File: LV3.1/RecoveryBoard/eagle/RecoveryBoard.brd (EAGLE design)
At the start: 120.9 x 54.6 mm, 88 parts, among them IC1 BD62120AEFJ-E2, Q6 MOSFET-PCH-SOT23-6, U1 STM32F042K6, U10 TPS63070, Y1 ECS-160-10-36Q-ES-TR

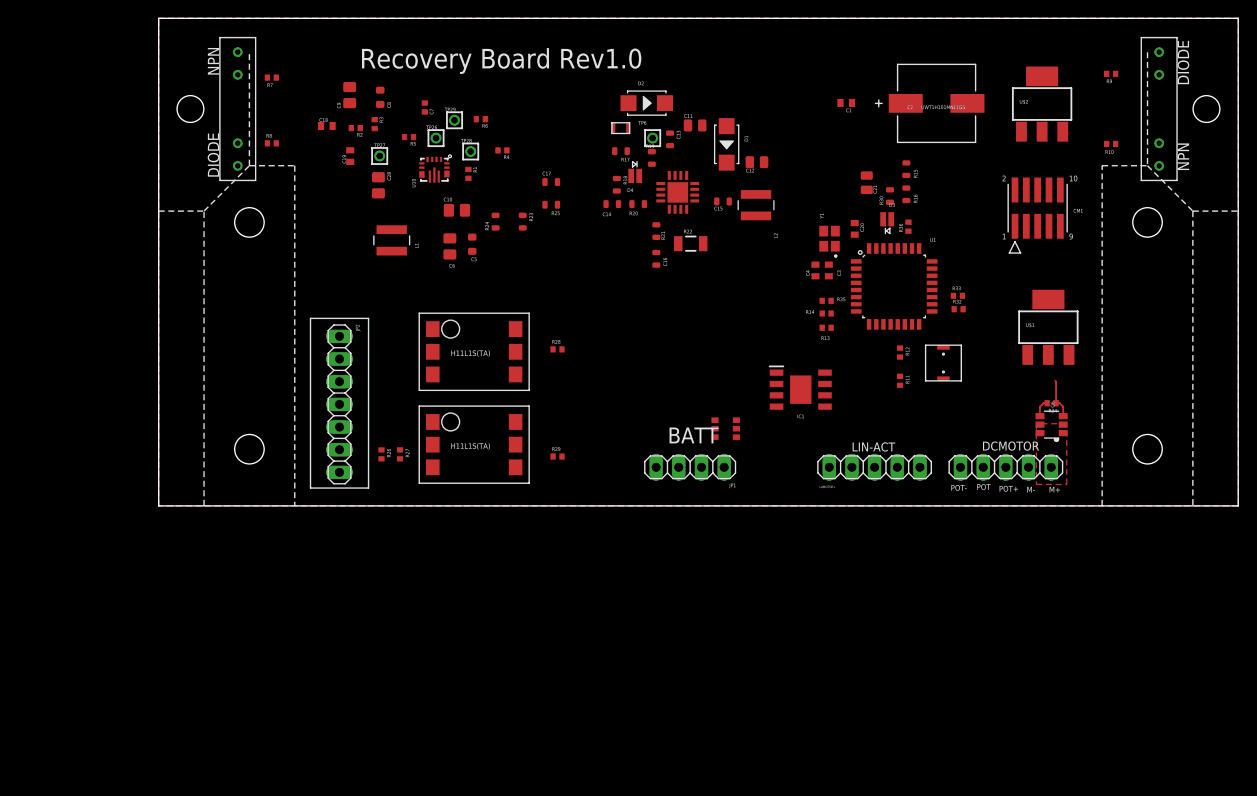
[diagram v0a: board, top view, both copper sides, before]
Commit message: OCD on package sizes 0603 for normal caps and resistors; 0805 for large caps, and larger yet for larger caps.
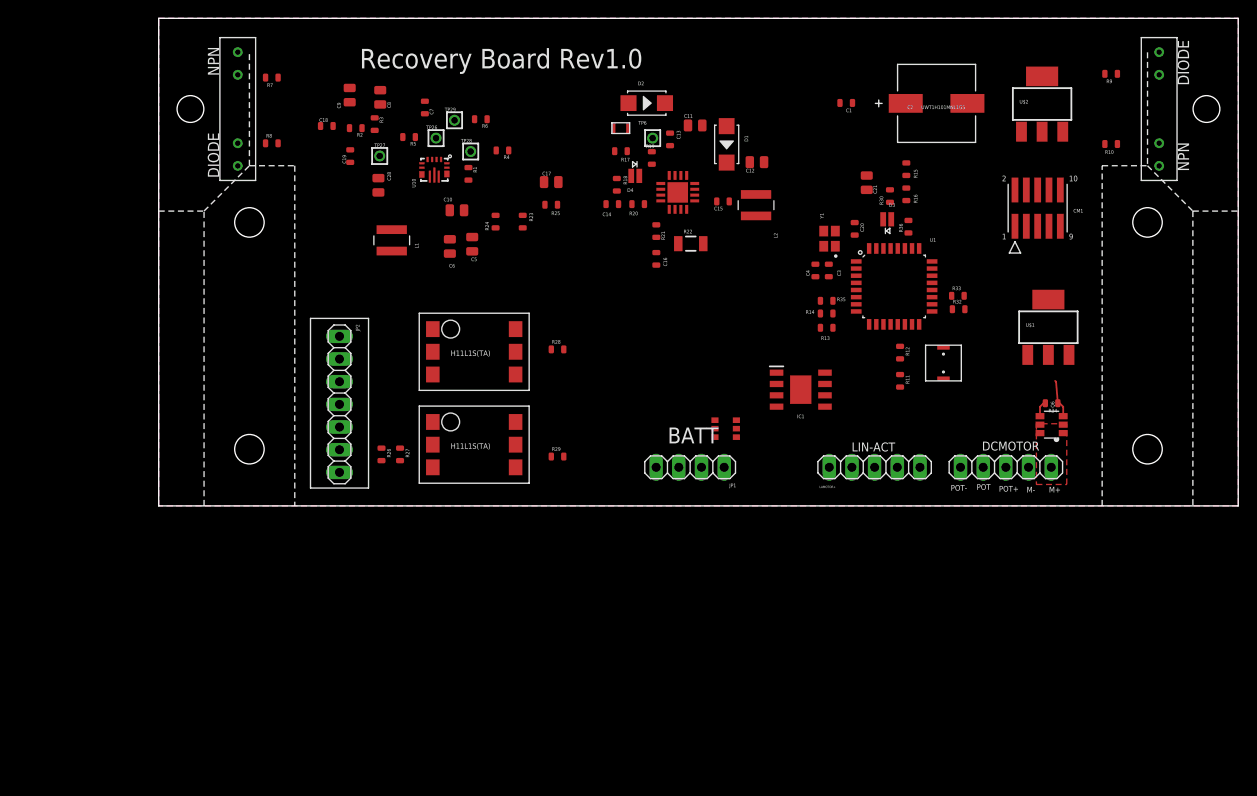
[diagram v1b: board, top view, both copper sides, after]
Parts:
- C1, C18, C19, C20, C3, C4: device rcl:C0402 -> oresat-rcl:.0603-C-NOSILK
- C10, C28, C6, C9: device oresat-rcl:.0805-B-NOSILK -> oresat-rcl:.0805-C-NOSILK
- C17: device oresat-rcl:.0603-C-NOSILK -> oresat-rcl:.0805-C-NOSILK
- C5, C8: device oresat-rcl:.0603-B-NOSILK -> oresat-rcl:.0805-C-NOSILK
- C7, R1, R2, R3, R4, R5, R6: device rcl_custom:.0402-B-NOSILK -> oresat-rcl:.0603-C-NOSILK
- R10, R11, R12, R13, R14, R26, R27, R28, R29, R32, R33, R34, R35, R36, R7, R8, R9: device rcl:R0402 -> oresat-rcl:.0603-C-NOSILK

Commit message: beginning routing and placement
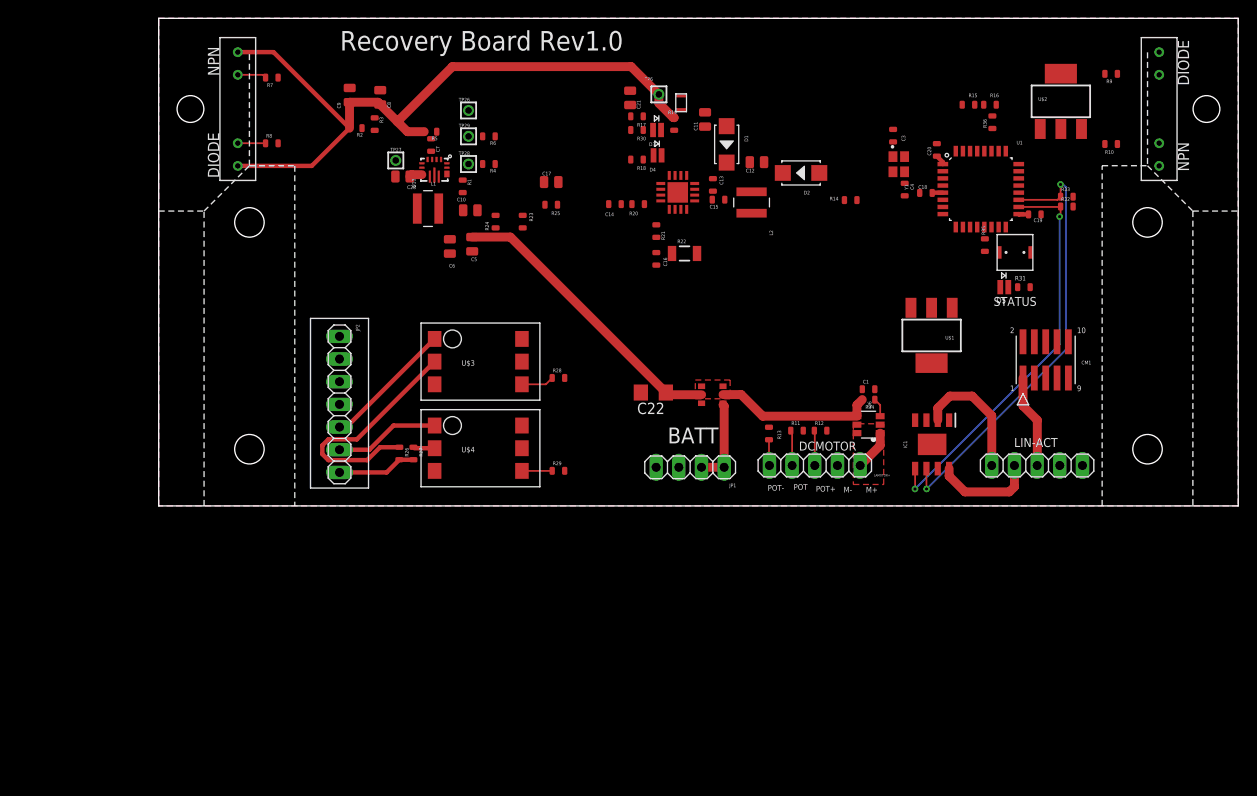
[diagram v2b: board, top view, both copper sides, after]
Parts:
- removed C2: UWT1H101MNL1GS, UWT1H101MNL1GS:PCAP_8X10-ELECT
- added C22: 100uF, oresat-rcl:C1206
- added D5: X-QE, D-Cree-XQE-LED:X-QE
- added R31: 220, oresat-rcl:.0603-C-NOSILK
- U$3, U$4: value H11L1S(TA) -> H11F1SR2M; device Q--H11L1S(TA)--OptoIsolator:H11L1S(TA) -> Q--H11F1SR2M--OptoIsolator:H11F1SR2M
- moved C19 76.9 mm to (98.1, 32.6), turned to 0 degrees
- moved C18 67.5 mm to (85.9, 35.0)
- moved C1 32.2 mm to (79.5, 13.1), turned to 0 degrees
- moved R30 29.3 mm to (53.6, 42.1), turned to 180 degrees
- moved C21 28.2 mm to (52.8, 45.7)
- moved D3 27.6 mm to (55.8, 42.1), turned to 0 degrees
- moved J1 21.4 mm to (73.5, 4.53)
- moved R34 20.5 mm to (79.5, 11.9)
- moved Q6 20.5 mm to (79.5, 9.10)
- moved D2 19.0 mm to (71.9, 37.3), turned to 180 degrees
- moved R35 18.8 mm to (92.5, 29.2), turned to 270 degrees
- moved J2 18.2 mm to (98.4, 4.53)
- moved CM1 17.0 mm to (99.3, 16.4)
- moved C3 16.7 mm to (82.2, 41.5)
- moved R32 16.7 mm to (101.7, 33.5)
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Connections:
- removed net LED: U1.26
- removed net N$25: R28.1, U$3.GND
- removed net N$29: R29.1, U$4.GND
- new net N$15: D5.ANODE, U1.14
- new net N$4: D5.CATHODE, R31.1
- net +12V: now also C22.1; no longer C2.1
- net 3.3V: now also U$3.IN, U$4.IN; no longer U$3.VCC, U$4.VCC
- net ARM-IN: now also JP2.2; no longer JP2.6
- net ARM-OUT: now also JP2.1; no longer JP2.7
- net CHUTE: now also JP2.5; no longer JP2.3
- net DCMDIR: no longer U1.13
- net DCM_ON: now also U1.13; no longer U1.6
- net DCM_PWM: no longer U1.14
- net DCM_SPEED: now also U1.6; no longer U1.7
- net DROGUE: now also JP2.6; no longer JP2.4
- net GND: now also C22.2, JP2.4, R31.2; no longer C2.2, JP2.2
- net ISO-CHUTE: now also R28.1, U$3.OUT, U1.9; no longer U$3.VO, U1.11
- net ISO-DROGUE: now also R29.1, U$4.OUT, U1.10; no longer U$4.VO, U1.12
- net SENSOR1: no longer U1.9
- net SENSOR2: no longer U1.10
- net T_GND: now also JP2.7; no longer JP2.5
- net VUMB: now also JP2.3; no longer JP2.1
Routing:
- net 3.3V: track 0.00 -> 94.8 mm
- net IN2: track 0.00 -> 49.5 mm, vias 0 -> 2
- net +12V: track 1.82 -> 51.1 mm
- net IN1: track 0.00 -> 45.4 mm, vias 0 -> 2
- net N$7: track 0.00 -> 26.9 mm
- net CHUTE: track 0.00 -> 14.7 mm
- net LAMOTOR+: track 0.00 -> 14.4 mm
- net DROGUE: track 0.00 -> 11.8 mm
- net LAMOTOR-: track 0.00 -> 11.5 mm
- net VBAT: track 0.00 -> 9.58 mm
- net T_GND: track 0.00 -> 8.87 mm
- net DCM+: track 0.00 -> 4.55 mm
- net DCM_PWM: track 0.00 -> 3.97 mm
- net DCMDIR: track 0.00 -> 3.93 mm
- net ISO-CHUTE: track 0.00 -> 3.68 mm
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- added copper zone on layer 1, net +12V
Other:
- board text added: "STATUS"
- board text removed: "SPS"
- board text removed: "this cap is too big"

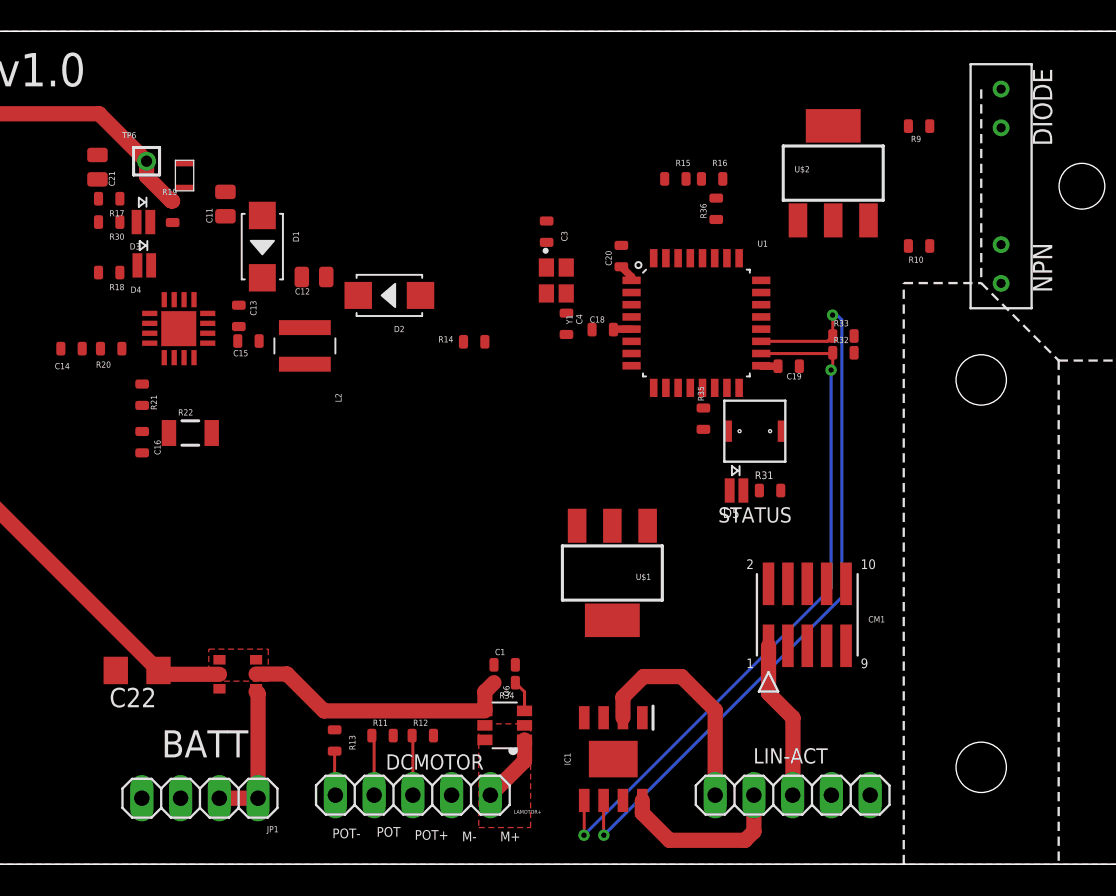
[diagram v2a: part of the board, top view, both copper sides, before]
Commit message: beginning routing and placement
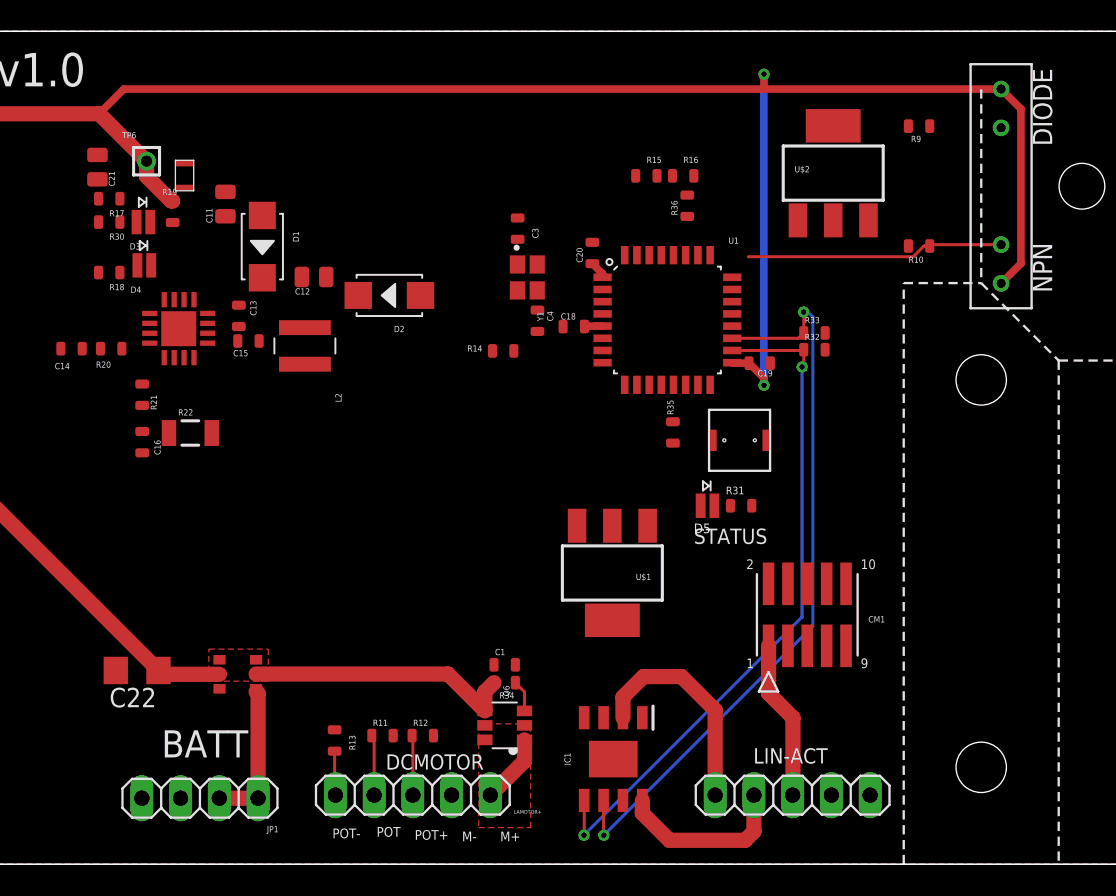
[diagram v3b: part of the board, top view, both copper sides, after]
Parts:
- moved R35 2.19 mm to (90.5, 28.3)
- moved D5 2.15 mm to (92.8, 23.5)
- moved R31 2.15 mm to (95.0, 23.5)
- moved R14 1.99 mm to (79.4, 33.6)
- moved C18 1.91 mm to (84.0, 35.2)
- moved C19 1.91 mm to (96.2, 32.9)
- moved C20 1.91 mm to (85.2, 40.1)
- moved C3 1.91 mm to (80.3, 41.7)
- moved R36 1.91 mm to (91.5, 43.2)
- moved Y1 1.91 mm to (81.0, 38.5)
- moved C4 1.91 mm to (81.7, 35.6)
- moved R15 1.91 mm to (88.8, 45.1)
- moved R16 1.91 mm to (91.2, 45.1)
- moved U1 1.91 mm to (90.2, 35.7)
- moved R32 1.91 mm to (99.8, 33.7)
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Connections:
- net BATT_READ: now also U1.29; no longer U1.28
- net DCMDIR: now also U1.12
- net DCM_PWM: now also U1.11
- net SENSOR1: now also U1.28
- net SENSOR2: now also U1.27
- net SENSOR_ON: now also U1.26; no longer U1.27
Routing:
- net 3.3V: track 94.8 -> 191.7 mm, vias 0 -> 2
- net SENSOR2: track 0.00 -> 16.9 mm
- net IN1: track 45.4 -> 44.8 mm
- net IN2: track 49.5 -> 48.9 mm

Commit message: finished routing
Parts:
- moved C20 0.53 mm to (85.8, 40.0), turned to 0 degrees
- moved C5 0.36 mm to (35.3, 29.0)
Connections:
- net N$3 renamed OSC_IN
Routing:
- net N$27: track 0.00 -> 131.4 mm, vias 0 -> 2
- net 3.3V: track 191.7 -> 313.9 mm, vias 2 -> 3
- net VBAT: track 9.58 -> 109.3 mm, vias 0 -> 4
- net SENSOR1: track 3.24 -> 89.3 mm, vias 0 -> 2
- net VUMB: track 0.00 -> 73.1 mm, vias 0 -> 1
- net ISO-DROGUE: track 3.39 -> 62.4 mm, vias 0 -> 2
- net POT_OUT_AN: track 0.00 -> 57.9 mm
- net ISO-CHUTE: track 3.68 -> 54.9 mm, vias 0 -> 2
- net ACOK: track 0.00 -> 45.2 mm, vias 0 -> 2
- net DCM_SPEED: track 0.00 -> 36.8 mm, vias 0 -> 2
- net NRST: track 0.00 -> 35.8 mm, vias 0 -> 2
- net N$16: track 0.00 -> 34.1 mm, vias 0 -> 2
- net ARM-OUT: track 0.00 -> 32.3 mm, vias 0 -> 2
- net DCM_PWM: track 3.97 -> 34.5 mm, vias 0 -> 2
- net DCMDIR: track 3.93 -> 33.7 mm, vias 0 -> 2
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
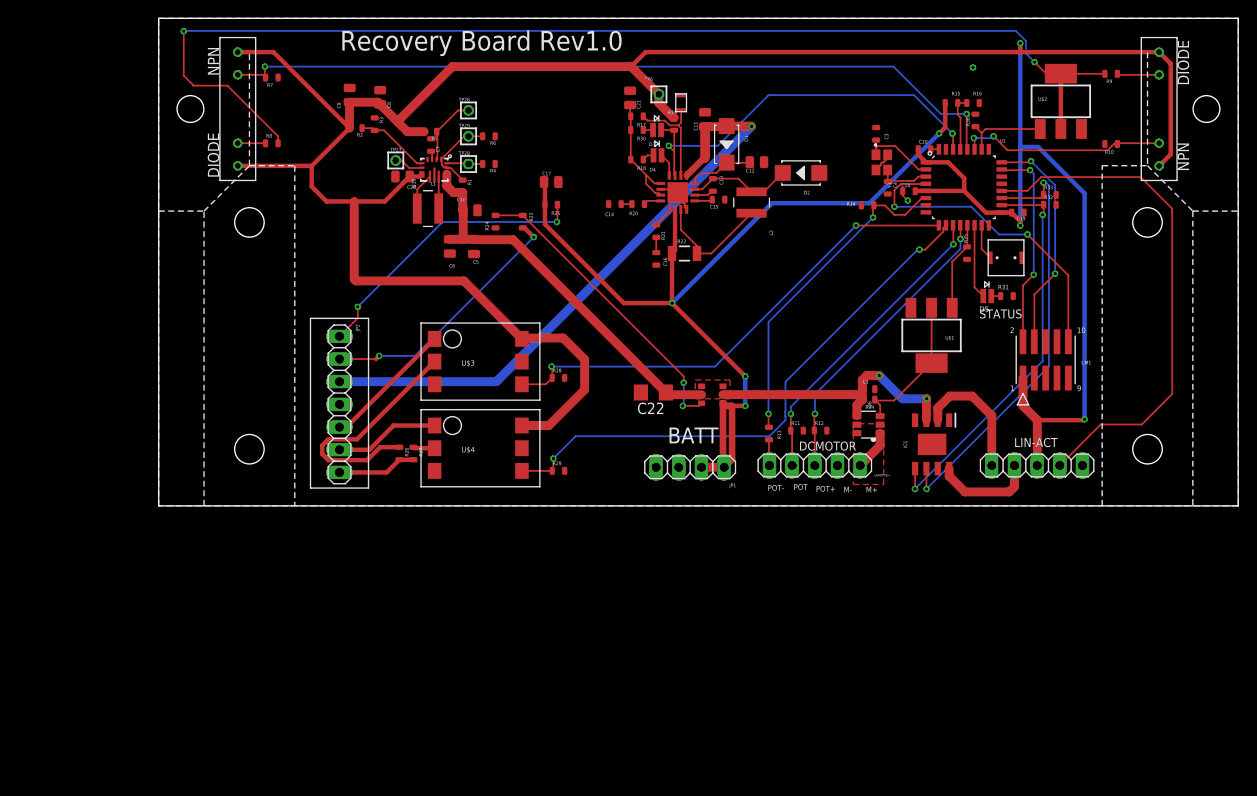
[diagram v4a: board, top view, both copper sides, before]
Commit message: finished routing and added TODO list
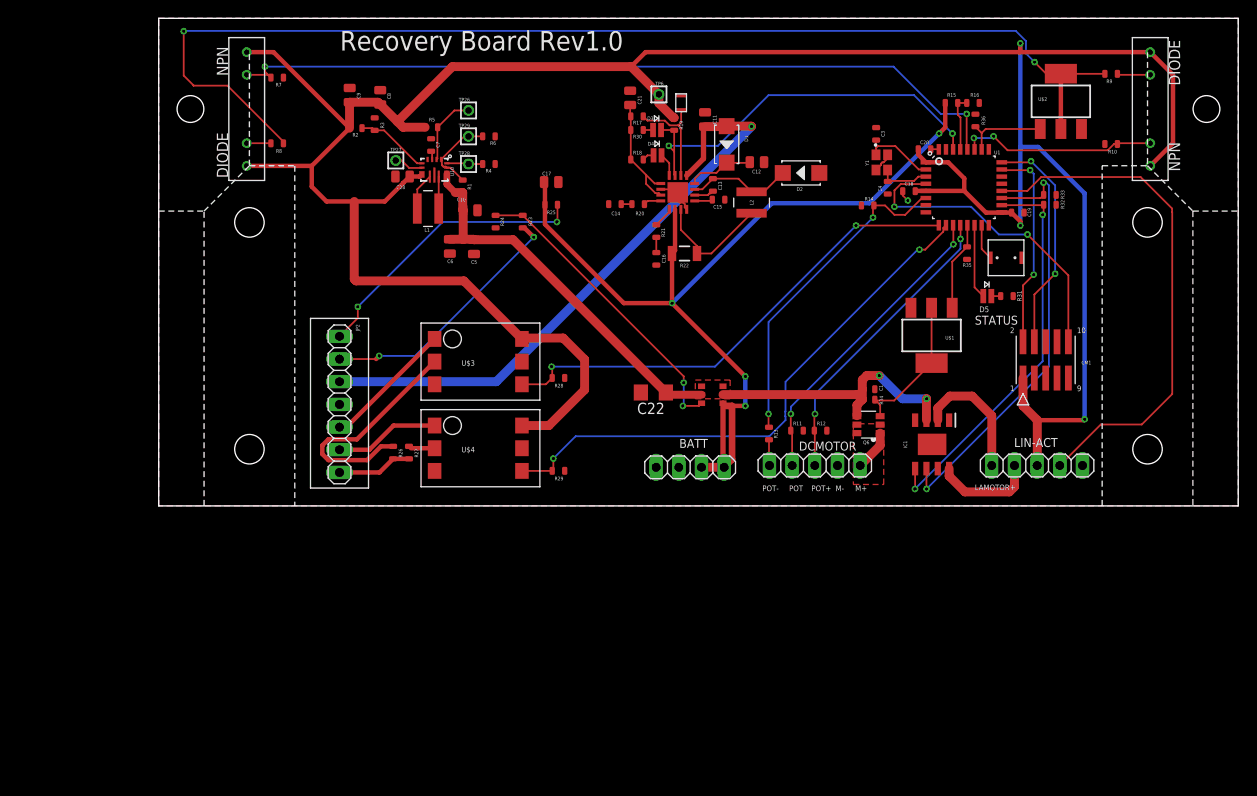
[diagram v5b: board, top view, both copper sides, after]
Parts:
- moved SENSOR 1.00 mm to (9.86, 44.5)
- moved SENSOR2 1.00 mm to (111.0, 44.5)
- moved R26 0.71 mm to (26.2, 5.97)
- moved R7 0.60 mm to (13.3, 48.0)
- moved R8 0.60 mm to (13.3, 40.6)
- moved R27 0.51 mm to (28.0, 5.97)
- moved R5 0.51 mm to (30.5, 42.4)
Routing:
- net VUMB: track 73.1 -> 69.6 mm
- net 3.3V: track 313.9 -> 311.8 mm
- net SENSOR2: track 23.1 -> 22.1 mm
- net N$5: track 4.72 -> 3.72 mm
- net N$7: track 26.9 -> 26.3 mm
- net N$26: track 2.42 -> 2.96 mm
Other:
- board text added: "3.3 SPS"
- board text added: "TODO 1. I have CAN and USART Pins currenlty doing nothing 2. Need to add locking button 3. Update Pin descriptions from schematic"
- board text added: "is this dumb?"

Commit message: More destruction on Ben's nice board. Good job Ben for putting up with Andrew.
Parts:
- removed U$1, U$2: NCH-SOT223, Q-MOSFET-NCH-SOT223:SOT223
- added Q1, Q2, Q3: BSS123, transistor-small-signal:SOT23
- added R37: 10k, oresat-rcl:.0603-C-NOSILK
- D3, D4, D5: value X-QE -> (none); device D-Cree-XQE-LED:X-QE -> led:CHIPLED_0603
- R18, R30: value (none) -> 1k
- R31: value 220 -> 1k
- moved C7 0.82 mm to (29.8, 40.0), turned to 180 degrees
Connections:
- net N$9 renamed !BEN
- new net N$1: Q1.3, U$7.NEG
- net 3.3V: now also U$7.POS
- net ACOK: now also D3.C; no longer D3.CATHODE
- net DCM_ON: now also Q3.1; no longer U$1.1
- net GND: now also IC1.9, Q1.2, Q2.2, Q3.2, R37.2; no longer U$1.3, U$2.3, U$7.NEG
- net N$13: now also D4.C; no longer D4.CATHODE
- net N$14: now also D3.A; no longer D3.ANODE
- net N$15: now also D5.A; no longer D5.ANODE
- net N$17: now also D4.A; no longer D4.ANODE
- net N$27: now also Q2.3; no longer U$2.2, U$2.4
- net N$4: now also D5.C; no longer D5.CATHODE
- net N$6: now also Q3.3; no longer U$1.2, U$1.4
- net N$8: now also Q1.1, R37.1; no longer U$7.POS
- net SENSOR_ON: now also Q2.1; no longer U$2.1
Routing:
- net VBAT: track 109.3 -> 92.4 mm
- net N$6: track 16.3 -> 9.45 mm, vias 0 -> 1
- net N$27: track 131.6 -> 125.4 mm
- net SENSOR_ON: track 9.57 -> 3.45 mm
- net DCM_ON: track 9.94 -> 4.78 mm
- net N$8: track 4.05 -> 2.66 mm
- net N$13: track 2.61 -> 3.47 mm
- net N$15: track 8.34 -> 9.19 mm
- net N$17: track 1.34 -> 2.02 mm
- net TPS-EN: track 9.44 -> 10.1 mm
- net 3.3V: track 311.8 -> 312.5 mm
- net N$4: track 1.05 -> 1.68 mm
- net N$14: track 1.09 -> 1.72 mm
- net ACOK: track 45.2 -> 45.8 mm
- net GND: vias 1 -> 9
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- added copper zone on layer 1, net VBAT
